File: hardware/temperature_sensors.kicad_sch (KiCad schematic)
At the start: 0 parts

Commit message: Add the Cube project
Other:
- title: Water Temperature Sensor -> Temperature Sensors
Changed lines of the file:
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@@
   (paper "A4")
   (title_block
-    (title "Water Temperature Sensor")
-    (date "2023-06-06")
+    (title "Temperature Sensors")
+    (date "2023-07-01")
     (rev "${REVISION}")
     (company "Author: I. Kajdan")

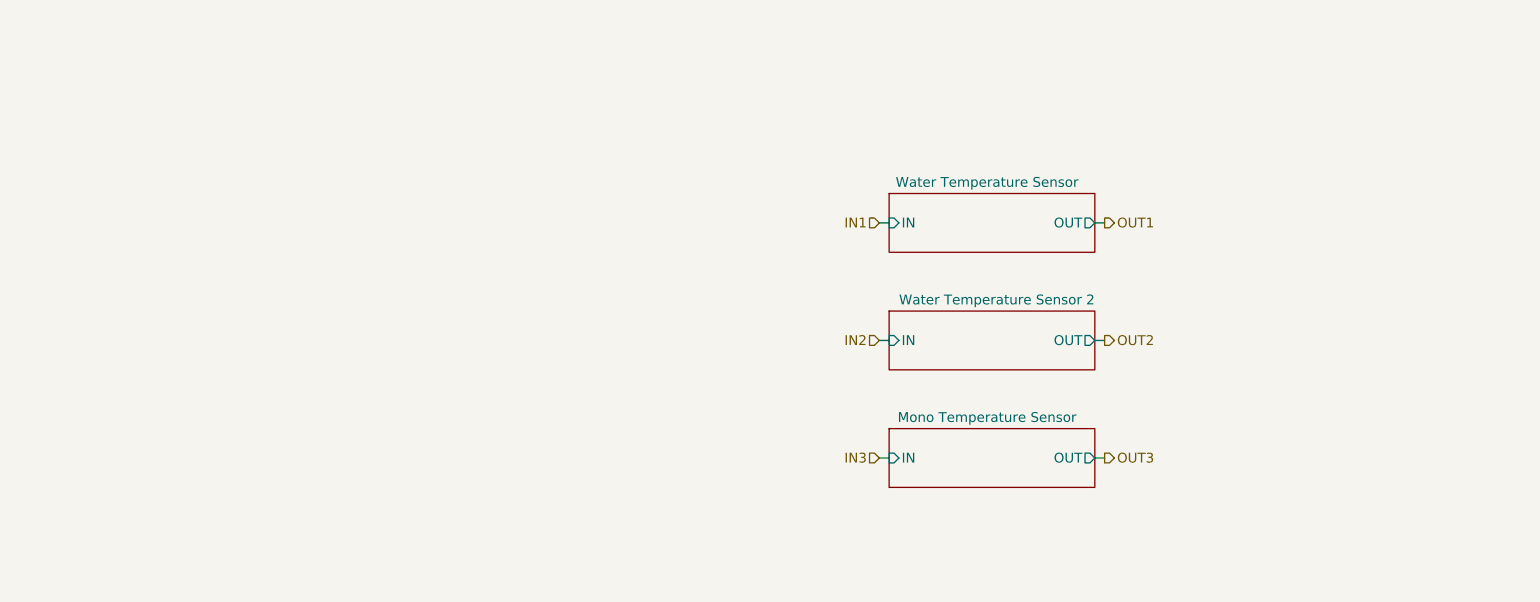
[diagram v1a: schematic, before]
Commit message: Improve the schematic
- add anti-aliasing filters
- rearrange the main connector signals
- improve the power filtering
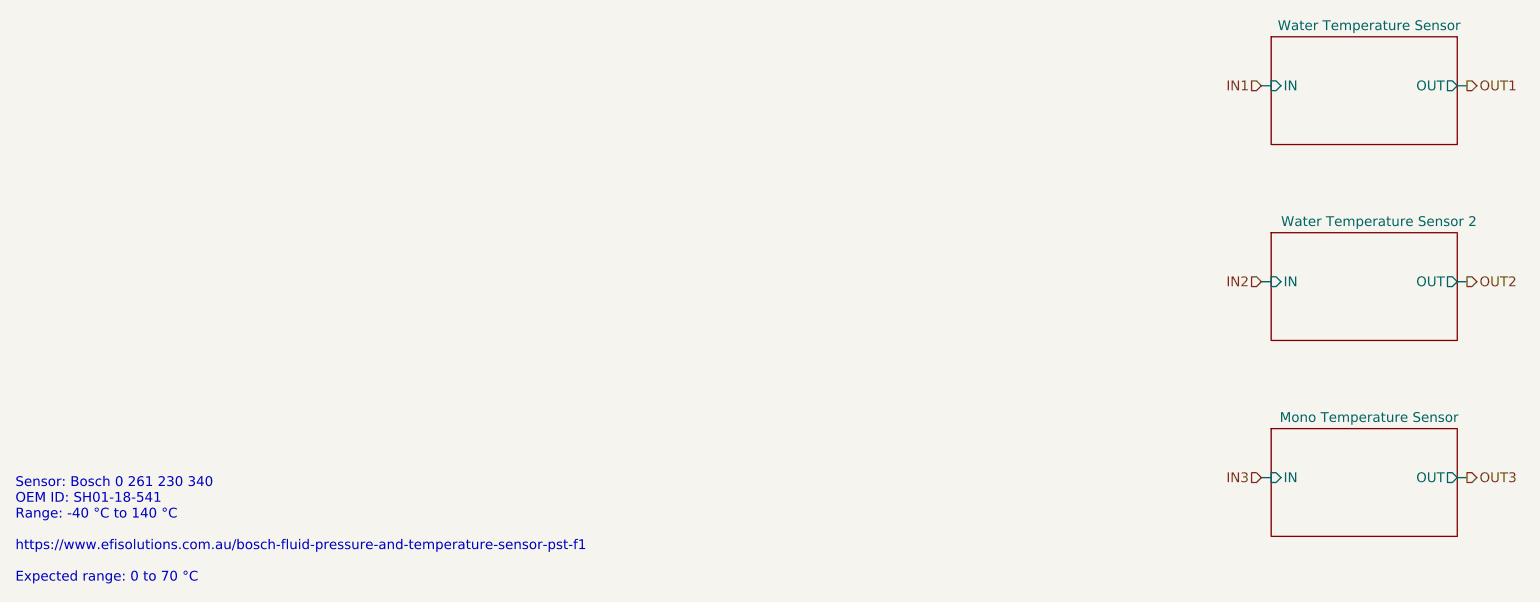
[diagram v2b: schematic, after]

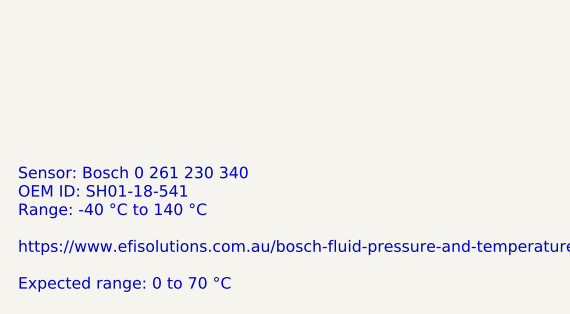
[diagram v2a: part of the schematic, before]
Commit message: Set component values
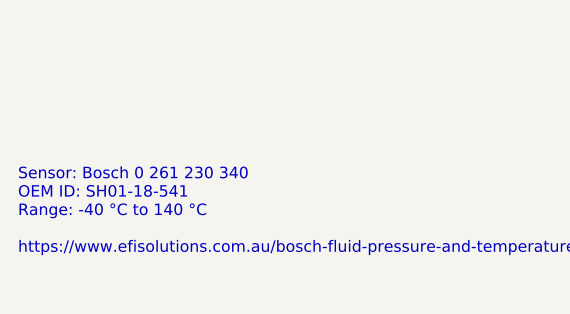
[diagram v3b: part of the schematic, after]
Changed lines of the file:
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@@
     )
   )
-  (text_box "Sensor: Bosch 0 261 230 340\nOEM ID: SH01-18-541\nRange: -40 °C to 140 °C\n\nhttps://www.efisolutions.com.au/bosch-fluid-pressure-and-temperature-sensor-pst-f1\n\nExpected range: 0 to 70 °C"
-    (at 22.86 115.57 0) (size 90.17 16.51)
+  (text_box "Sensor: Bosch 0 261 230 340\nOEM ID: SH01-18-541\nRange: -40 °C to 140 °C\n\nhttps://www.efisolutions.com.au/bosch-fluid-pressure-and-temperature-sensor-pst-f1"
+    (at 22.86 115.57 0) (size 90.17 11.43)
     (stroke (width -0.0001) (type default))
     (fill (type none))
